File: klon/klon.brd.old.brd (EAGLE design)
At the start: 160 x 100 mm, 14 parts, among them IC1 MAX1044

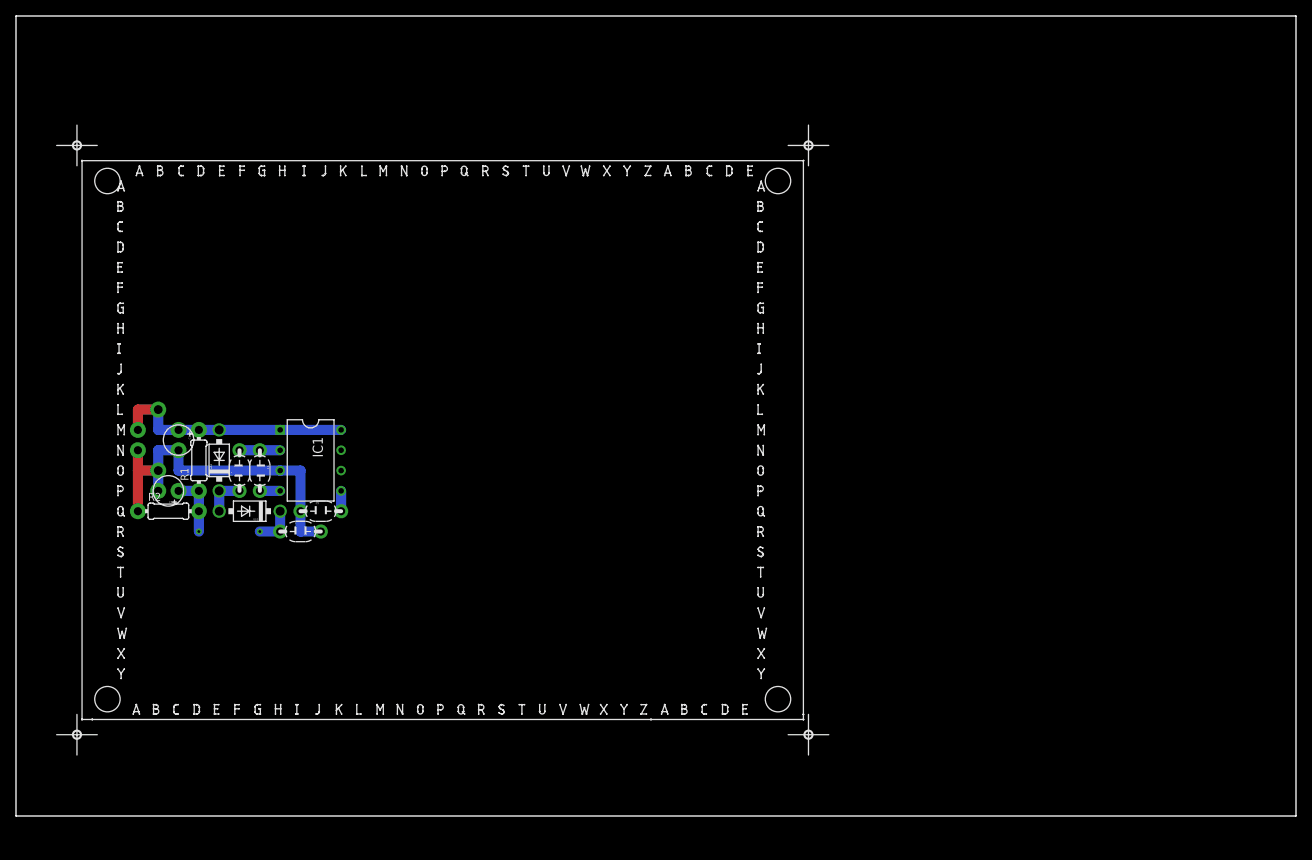
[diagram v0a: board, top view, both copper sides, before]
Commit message: Add klon power.
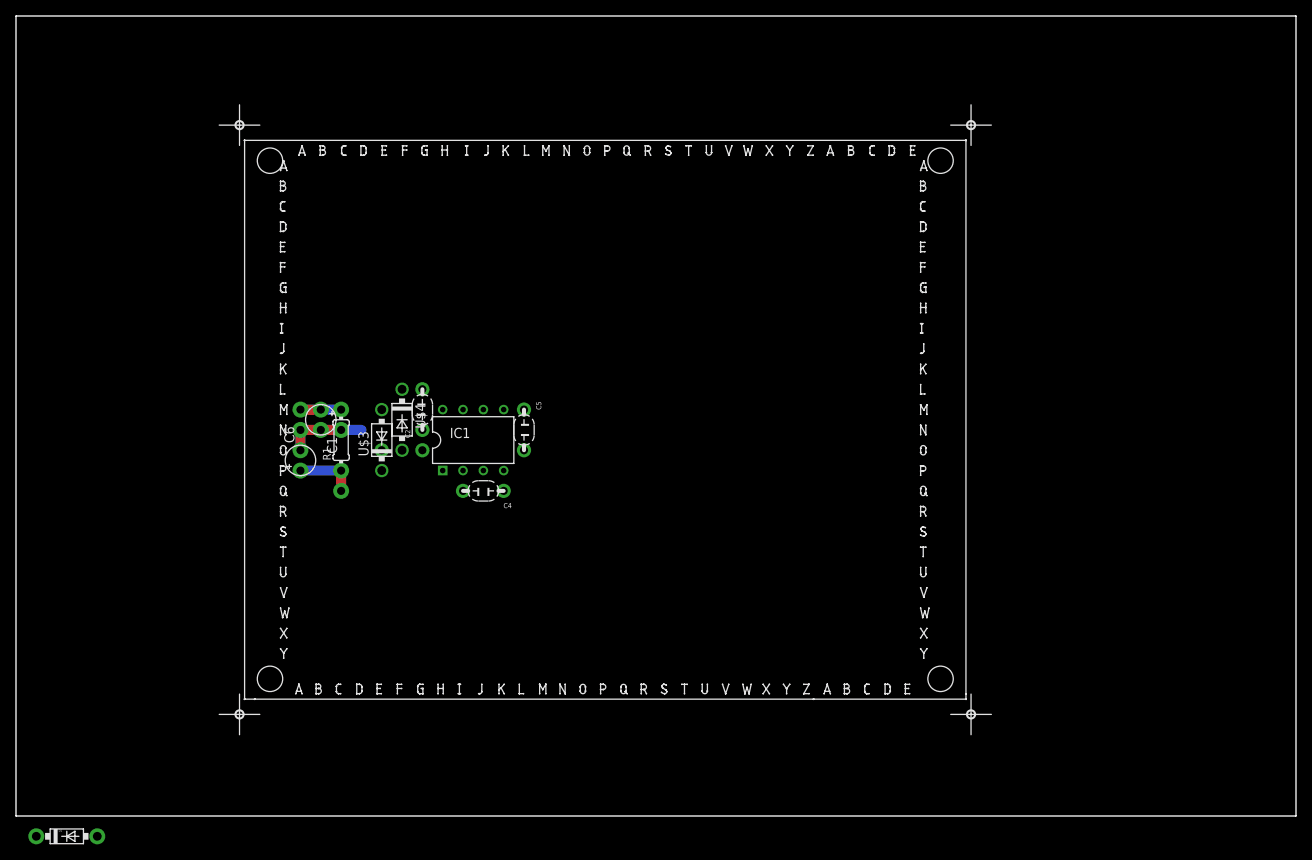
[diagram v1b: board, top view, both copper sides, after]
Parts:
- removed U$2: 2_1MM-JACK-PLUG, pedal-library:1X02
- added POWER: 2_1MM-JACK-PLUG, pedal-library:1X02
- C5: value 1u -> (none)
- D1: value 1N4742 -> 1N4742DO41-7.6
- moved D1 50.6 mm to (7.62, -2.54), flipped to the top, turned to 0 degrees
- moved C4 30.6 mm to (61.0, 40.6), turned to 180 degrees
- moved C5 28.4 mm to (63.5, 50.8), turned to 270 degrees
- moved U$4 24.5 mm to (48.3, 53.3), turned to 270 degrees
- moved R2 24.1 mm to (40.6, 45.7), flipped to the bottom, turned to 270 degrees
- moved C3 23.0 mm to (50.8, 45.7), flipped to the bottom, turned to 0 degrees
- moved IC1 20.5 mm to (57.1, 47.0), turned to 0 degrees
- moved U$1 20.5 mm to (25.4, 10.2)
- moved C2 19.8 mm to (50.8, 48.3), turned to 90 degrees
- moved C1 18.2 mm to (38.1, 50.8)
- moved R1 18.0 mm to (40.6, 45.7)
- moved U$3 17.3 mm to (45.7, 43.2), turned to 90 degrees
- moved C6 16.7 mm to (35.6, 43.2), turned to 90 degrees
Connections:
- net +16.2V: now also C2.2, U$4.C; no longer C2.1, U$3.C
- net +9V: now also POWER.2, U$3.A; no longer U$2.2, U$4.A
- net GND: now also C2.1, C5.2, POWER.1; no longer C2.2, C5.1, U$2.1
- net N$2: now also C5.1; no longer C5.2
- net N$3: now also C3.2, U$3.C, U$4.A; no longer C3.1, U$3.A, U$4.C
- net N$5: now also C4.1; no longer C4.2
- net N$6: now also C3.1, C4.2; no longer C3.2, C4.1
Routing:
- net GND: track 45.7 -> 10.2 mm
- net +9V: track 30.5 -> 5.08 mm
- net N$6: track 5.08 -> 0.00 mm
- net N$3: track 5.08 -> 0.00 mm
- net +16.2V: track 5.08 -> 0.00 mm, vias 1 -> 0
- net N$5: track 2.54 -> 0.00 mm
- net N$2: track 2.54 -> 0.00 mm
- net +4.5V: vias 1 -> 0
